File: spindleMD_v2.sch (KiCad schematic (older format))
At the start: 40 parts, among them J1 Conn_LogicPower, J2 Conn_SWD, J3 Conn_UART, J4 Conn_I2C, J5 Conn_Encoder, J6 Conn_GPIO, J7 Conn_MotorPower, J8 Conn_drivePower, J9 Conn_Motor, SW1 USER_BUTTON, SW2 RESET_BUTTON, U1 L7805, U2 L78L33_SOT89, U3 IK0505SA

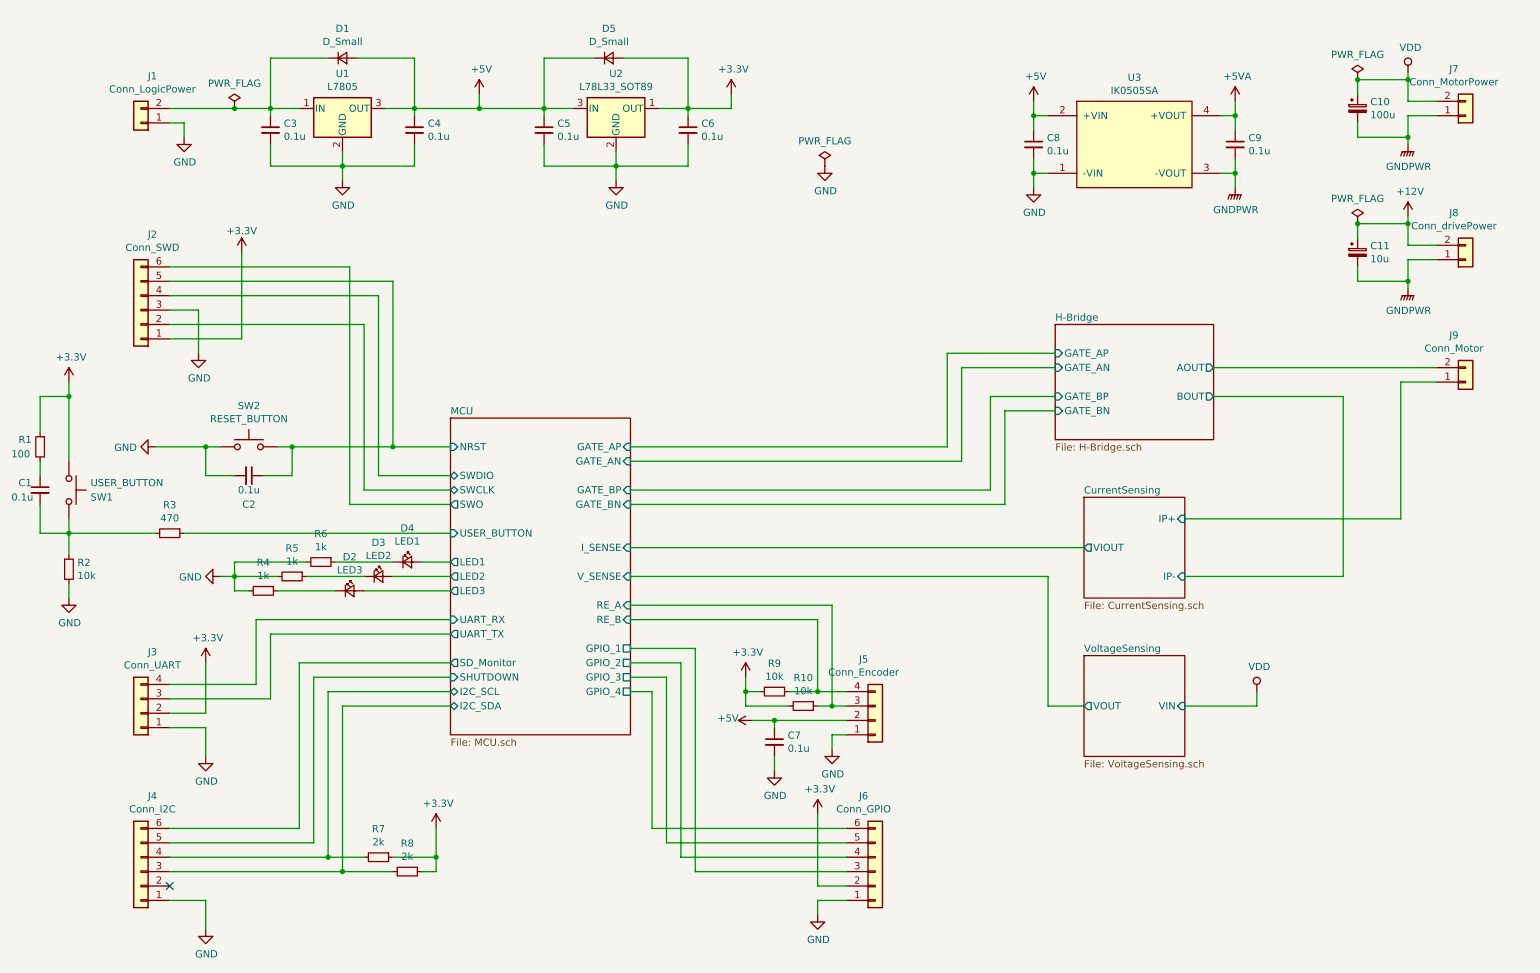
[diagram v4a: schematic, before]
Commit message: 電源LED追加
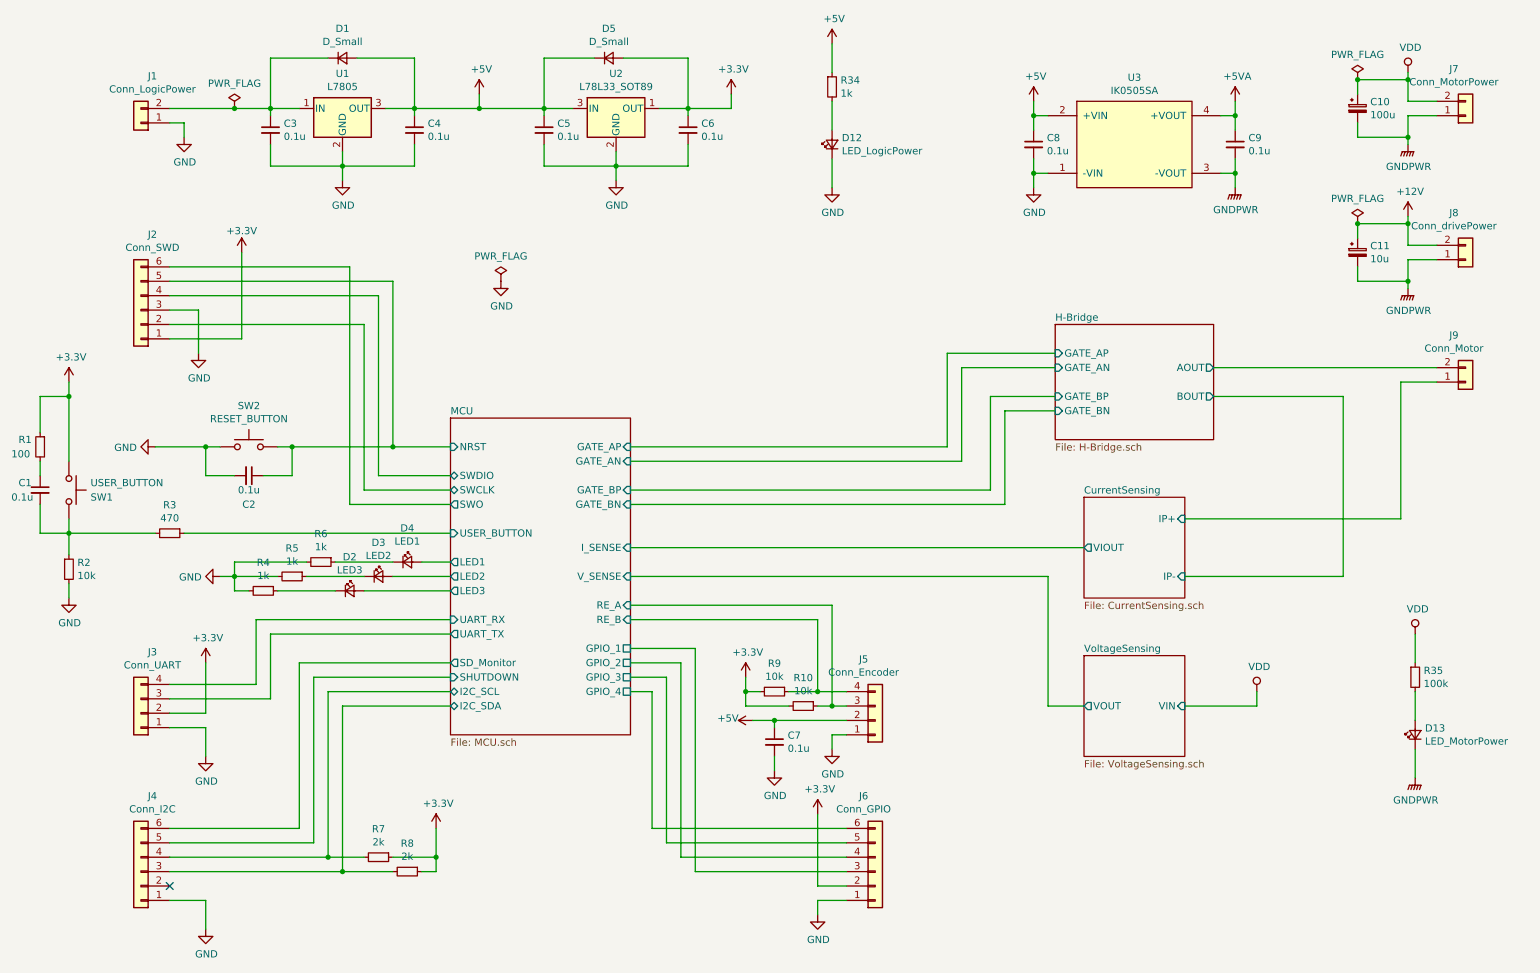
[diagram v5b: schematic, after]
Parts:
- added D12: LED_LogicPower, LEDs:LED_0603_HandSoldering, symbol Device:LED_Small
- added D13: LED_MotorPower, LEDs:LED_0603_HandSoldering, symbol Device:LED_Small
- added R34: 1k, Resistors_SMD:R_0603_HandSoldering, symbol Device:R_Small
- added R35: 100k, Resistors_SMD:R_0603_HandSoldering, symbol Device:R_Small
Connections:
- net +5V: now also R34.1
- net GND: now also D12.1 (K)
- net GNDPWR: now also D13.1 (K)
- net VDD: now also R35.1
- new net: D12.2 (A), R34.2
- new net: D13.2 (A), R35.2
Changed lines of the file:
@@
 L power:GND #PWR?
 U 1 1 5C7D9F11
-P 6300 1800
+P 4050 2600
 AR Path="/5C77D64E/5C7D9F11" Ref="#PWR?"  Part="1"
 AR Path="/5C7D9F11" Ref="#PWR0101"  Part="1"
-F 0 "#PWR0101" H 6300 1550 50  0001 C CNN
-F 1 "GND" H 6305 1627 50  0000 C CNN
-F 2 "" H 6300 1800 50  0001 C CNN
-F 3 "" H 6300 1800 50  0001 C CNN
-	1    6300 1800
+F 0 "#PWR0101" H 4050 2350 50  0001 C CNN
+F 1 "GND" H 4055 2427 50  0000 C CNN
+F 2 "" H 4050 2600 50  0001 C CNN
+F 3 "" H 4050 2600 50  0001 C CNN
+	1    4050 2600
 	1    0    0    -1
 $EndComp
@@
 L power:PWR_FLAG #FLG0102
 U 1 1 5C7F1DF2
-P 6300 1800
-F 0 "#FLG0102" H 6300 1875 50  0001 C CNN
-F 1 "PWR_FLAG" H 6300 1974 50  0000 C CNN
-F 2 "" H 6300 1800 50  0001 C CNN
-F 3 "~" H 6300 1800 50  0001 C CNN
-	1    6300 1800
+P 4050 2600
+F 0 "#FLG0102" H 4050 2675 50  0001 C CNN
+F 1 "PWR_FLAG" H 4050 2774 50  0000 C CNN
+F 2 "" H 4050 2600 50  0001 C CNN
+F 3 "~" H 4050 2600 50  0001 C CNN
+	1    4050 2600
 	1    0    0    -1
 $EndComp
@@
 $EndComp
 Connection ~ 10000 1200
+$Comp
+L power:GND #PWR0102
+U 1 1 5C7EC1F5
+P 6350 1950
+F 0 "#PWR0102" H 6350 1700 50  0001 C CNN
+F 1 "GND" H 6355 1777 50  0000 C CNN
+F 2 "" H 6350 1950 50  0001 C CNN
+F 3 "" H 6350 1950 50  0001 C CNN
+	1    6350 1950
+	1    0    0    -1
+$EndComp
+$Comp
+L Device:R_Small R34
+U 1 1 5C7EC340
+P 6350 1250
+F 0 "R34" H 6409 1296 50  0000 L CNN
+F 1 "1k" H 6409 1205 50  0000 L CNN
+F 2 "Resistors_SMD:R_0603_HandSoldering" H 6350 1250 50  0001 C CNN
+F 3 "~" H 6350 1250 50  0001 C CNN
+	1    6350 1250
+	1    0    0    -1
+$EndComp
+$Comp
+L Device:LED_Small D12
+U 1 1 5C7F7A68
+P 6350 1650
+F 0 "D12" V 6396 1582 50  0000 R CNN
+F 1 "LED_LogicPower" V 6305 1582 50  0000 R CNN
+F 2 "LEDs:LED_0603_HandSoldering" V 6350 1650 50  0001 C CNN
+F 3 "~" V 6350 1650 50  0001 C CNN
+	1    6350 1650
+	0    -1   -1   0
+$EndComp
+$Comp
+L power:+5V #PWR?
+U 1 1 5C7F7D3B
+P 6350 950
+AR Path="/5C77D686/5C7F7D3B" Ref="#PWR?"  Part="1"
+AR Path="/5C7F7D3B" Ref="#PWR0103"  Part="1"
+F 0 "#PWR0103" H 6350 800 50  0001 C CNN
+F 1 "+5V" H 6365 1123 50  0000 C CNN
+F 2 "" H 6350 950 50  0001 C CNN
+F 3 "" H 6350 950 50  0001 C CNN
+	1    6350 950
+	1    0    0    -1
+$EndComp
+Wire Wire Line
+	6350 950  6350 1150
+Wire Wire Line
+	6350 1350 6350 1550
+Wire Wire Line
+	6350 1750 6350 1950
+$Comp
+L Device:R_Small R35
+U 1 1 5C81A95A
+P 10400 5350
+F 0 "R35" H 10459 5396 50  0000 L CNN
+F 1 "100k" H 10459 5305 50  0000 L CNN
+F 2 "Resistors_SMD:R_0603_HandSoldering" H 10400 5350 50  0001 C CNN
+F 3 "~" H 10400 5350 50  0001 C CNN
+	1    10400 5350
+	1    0    0    -1
+$EndComp
+$Comp
+L Device:LED_Small D13
+U 1 1 5C81A961
+P 10400 5750
+F 0 "D13" V 10446 5682 50  0000 R CNN
+F 1 "LED_MotorPower" V 10355 5682 50  0000 R CNN
+F 2 "LEDs:LED_0603_HandSoldering" V 10400 5750 50  0001 C CNN
+F 3 "~" V 10400 5750 50  0001 C CNN
+	1    10400 5750
+	0    -1   -1   0
+$EndComp
+Wire Wire Line
+	10400 5050 10400 5250
+Wire Wire Line
+	10400 5450 10400 5650
+$Comp
+L power:GNDPWR #PWR?
+U 1 1 5C8264F0
+P 10400 6050
+AR Path="/5C77D64E/5C8264F0" Ref="#PWR?"  Part="1"
+AR Path="/5C8264F0" Ref="#PWR0104"  Part="1"
+F 0 "#PWR0104" H 10400 5850 50  0001 C CNN
+F 1 "GNDPWR" H 10404 5896 50  0000 C CNN
+F 2 "" H 10400 6000 50  0001 C CNN
+F 3 "" H 10400 6000 50  0001 C CNN
+	1    10400 6050
+	1    0    0    -1
+$EndComp
+Wire Wire Line
+	10400 5850 10400 6050
+$Comp
+L power:VDD #PWR?
+U 1 1 5C8323C8
+P 10400 5050
+AR Path="/5C77D64E/5C8323C8" Ref="#PWR?"  Part="1"
+AR Path="/5C8323C8" Ref="#PWR0105"  Part="1"
+F 0 "#PWR0105" H 10400 4900 50  0001 C CNN
+F 1 "VDD" H 10417 5223 50  0000 C CNN
+F 2 "" H 10400 5050 50  0001 C CNN
+F 3 "" H 10400 5050 50  0001 C CNN
+	1    10400 5050
+	1    0    0    -1
+$EndComp
 $EndSCHEMATC

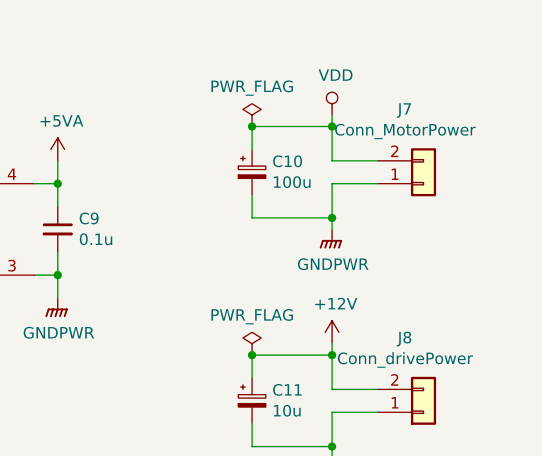
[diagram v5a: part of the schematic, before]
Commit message: パワー電源コネクタピン配置修正
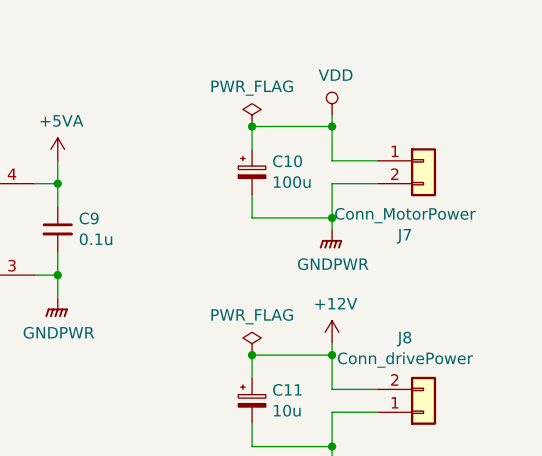
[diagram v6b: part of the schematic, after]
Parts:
- J2: footprint Connectors_JST:JST_XH_B06B-XH-A_06x2.50mm_Straight -> Connectors_JST:JST_PH_B6B-PH-K_06x2.00mm_Straight
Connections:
- net GNDPWR: now also J7.2 (Pin_2); no longer J7.1 (Pin_1)
- net VDD: now also J7.1 (Pin_1); no longer J7.2 (Pin_2)
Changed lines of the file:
@@
 F 0 "J2" H 1470 2275 50  0000 C CNN
 F 1 "Conn_SWD" H 1470 2366 50  0000 C CNN
-F 2 "Connectors_JST:JST_XH_B06B-XH-A_06x2.50mm_Straight" H 1550 2800 50  0001 C CNN
+F 2 "Connectors_JST:JST_PH_B6B-PH-K_06x2.00mm_Straight" H 1550 2800 50  0001 C CNN
 F 3 "~" H 1550 2800 50  0001 C CNN
 	1    1550 2800
@@
 L Connector_Generic:Conn_01x02 J7
 U 1 1 5CA3C517
-P 10750 1450
-F 0 "J7" H 10669 1125 50  0000 C CNN
-F 1 "Conn_MotorPower" H 10669 1216 50  0000 C CNN
-F 2 "Connectors_JST:JST_VH_B2P-VH-B_2x3.96mm_Vertical" H 10750 1450 50  0001 C CNN
-F 3 "~" H 10750 1450 50  0001 C CNN
-	1    10750 1450
-	1    0    0    1
-$EndComp
-Wire Wire Line
+P 10750 1350
+F 0 "J7" H 10669 1025 50  0000 C CNN
+F 1 "Conn_MotorPower" H 10669 1116 50  0000 C CNN
+F 2 "Connectors_JST:JST_VH_B2P-VH-B_2x3.96mm_Vertical" H 10750 1350 50  0001 C CNN
+F 3 "~" H 10750 1350 50  0001 C CNN
+	1    10750 1350
+	1    0    0    -1
+$EndComp
+Wire Wire Line
